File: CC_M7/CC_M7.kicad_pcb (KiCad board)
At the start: 4 copper layers, 40 x 65 mm, 118 parts, among them J1 Conn_01x04_Pin, J10 Conn_01x04_Pin, J11 USB_B_Micro, J12 Conn_01x04_Pin, J3 Conn_01x03_Pin, J4 Conn_01x03_Pin, J5 Conn_01x03_Pin, J6 Conn_01x03_Pin, J7 Conn_01x03_Pin, J8 Conn_01x03_Pin, U1 STM32H743VITx, U10 ME6211C33M5, U11 BMP581, U12 IIM-42652, U2 24AA64T-I/OT, U3 BMI088, U4 ICP-20100, U5 BMM150, U6 nRF52820-QDxx, U7 NRF21540-QDAA-R7, U8 TPS562246DRLR, U9 ME6211C33M5, Y1 32MHz, Y2 32MHz

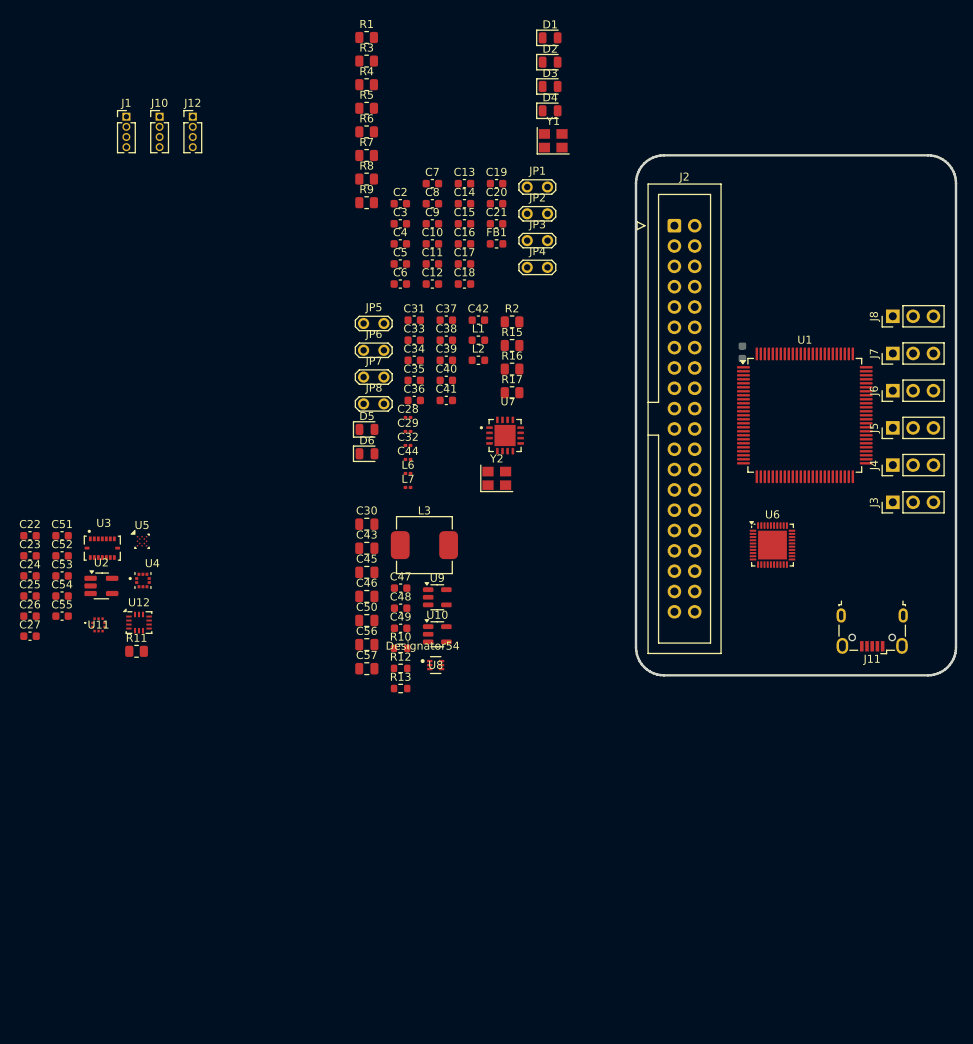
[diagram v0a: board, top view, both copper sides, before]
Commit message: nRF PCB placement completed
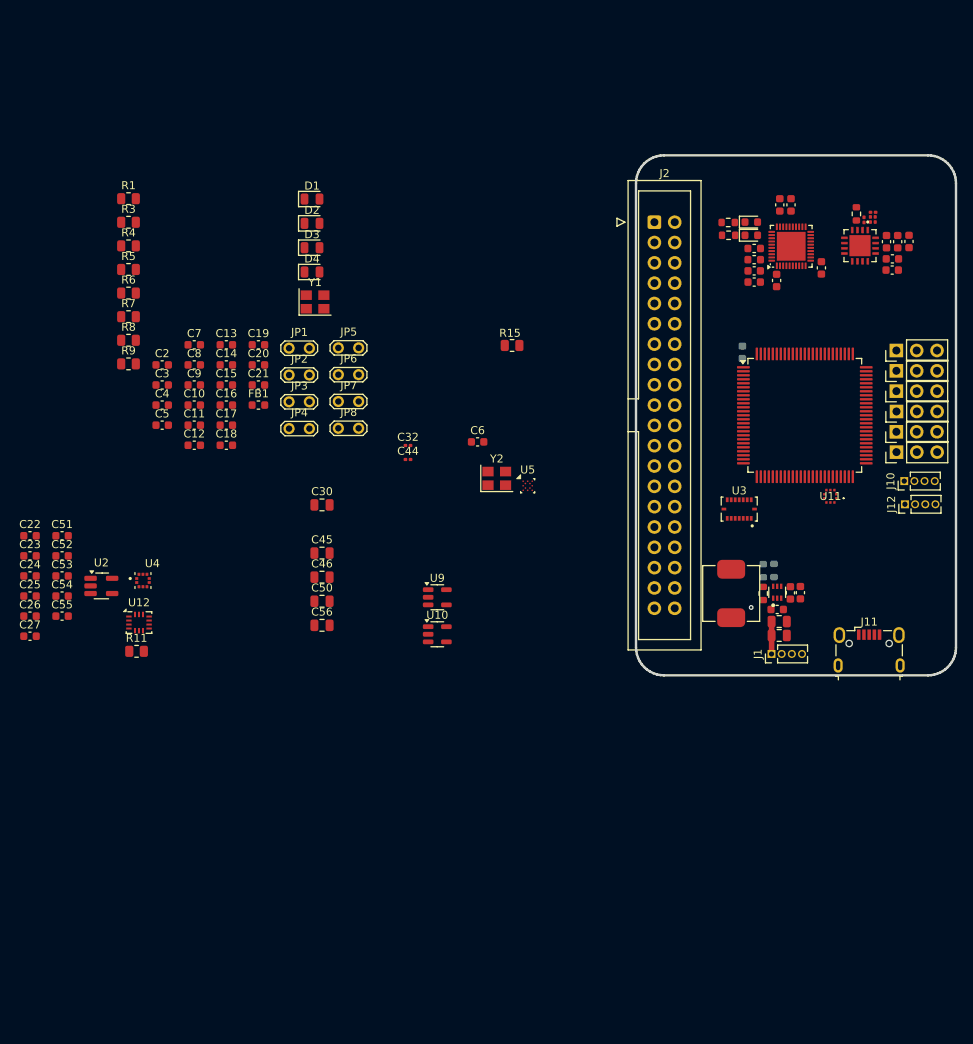
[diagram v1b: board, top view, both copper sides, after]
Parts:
- D5, D6: footprint LED_SMD:LED_0805_2012Metric -> LED_SMD:LED_0603_1608Metric
- R12, R13: moved to B.Cu
- R16, R17, R2: footprint Resistor_SMD:R_0805_2012Metric -> Resistor_SMD:R_0603_1608Metric
- moved J1 104.9 mm to (129.5, 130.8), turned to 90 degrees
- moved J10 103.6 mm to (146.1, 109.2), turned to 90 degrees
- moved J12 101.4 mm to (146.2, 112.1), turned to 90 degrees
- moved U11 92.9 mm to (136.9, 111.1), turned to 180 degrees
- moved U3 79.8 mm to (125.5, 112.7), turned to 180 degrees
- moved L7 66.8 mm to (141.9, 76.5), turned to 90 degrees
- moved L6 65.2 mm to (141.1, 76.5), turned to 90 degrees
- moved C29 64.3 mm to (142.2, 75.6)
- moved C28 63.4 mm to (142.5, 76.5), turned to 90 degrees
- moved C38 59.1 mm to (146.7, 79.2), turned to 90 degrees
- moved C40 59.0 mm to (145.3, 79.3), turned to -90 degrees
- moved C41 58.1 mm to (144.6, 82.8)
- moved C39 57.0 mm to (143.9, 79.3), turned to -90 degrees
- moved D6 56.1 mm to (127.0, 76.8)
- moved D5 53.8 mm to (127.0, 78.5)
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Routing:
- net +BATT: track 0.00 -> 4.16 mm
- net (no net): vias 0 -> 1

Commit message: Component placement completed
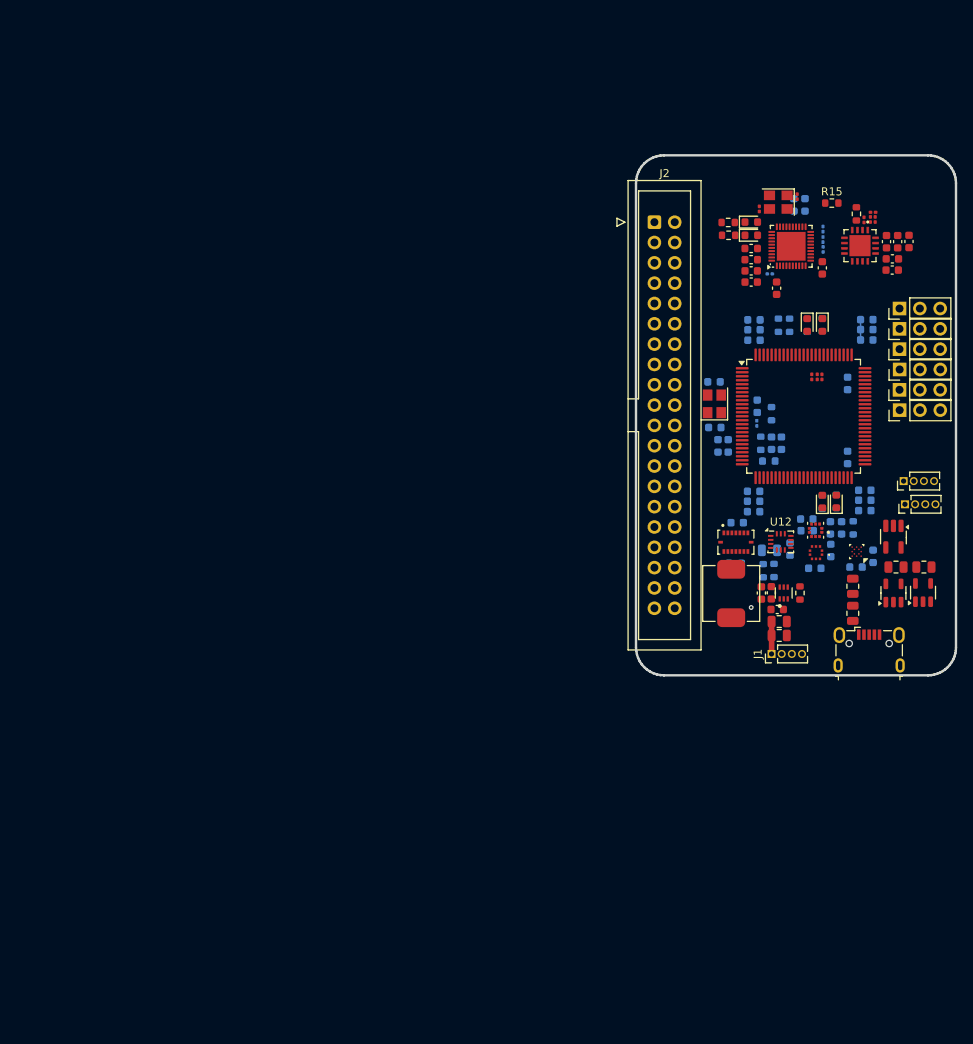
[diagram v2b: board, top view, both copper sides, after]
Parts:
- C10, C11, C12, C13, C14, C15, C16, C17, C18, C19, C2, C20, C21, C22, C23, C24, C25, C26, C27, C3, C31, C37, C4, C5, C51, C52, C53, C54, C55, C56, C6, C7, C8, C9, FB1: moved to B.Cu
- D1, D2, D3, D4: footprint LED_SMD:LED_0805_2012Metric -> LED_SMD:LED_0603_1608Metric
- JP1, JP2, JP3: footprint TestPoint:TestPoint_2Pads_Pitch2.54mm_Drill0.8mm -> Capacitor_SMD:C_0201_0603Metric
- JP4, JP5, JP6, JP7, JP8: footprint TestPoint:TestPoint_2Pads_Pitch2.54mm_Drill0.8mm -> Capacitor_SMD:C_0201_0603Metric; moved to B.Cu
- R1, R11, R3, R4, R5, R6, R7, R8, R9: footprint Resistor_SMD:R_0805_2012Metric -> Resistor_SMD:R_0603_1608Metric; moved to B.Cu
- R15: footprint Resistor_SMD:R_0805_2012Metric -> Resistor_SMD:R_0603_1608Metric
- moved C27 105.9 mm to (142.2, 118.6), turned to -90 degrees
- moved C26 103.4 mm to (140.1, 120.0)
- moved C23 101.5 mm to (138.3, 115.0), turned to -90 degrees
- moved C25 100.4 mm to (136.9, 115.0), turned to 90 degrees
- moved U2 99.2 mm to (144.8, 116.2), turned to -90 degrees
- moved C54 96.3 mm to (136.9, 117.9), turned to 90 degrees
- moved C55 94.3 mm to (134.9, 120.1), turned to 180 degrees
- moved C52 93.2 mm to (133.9, 114.0)
- moved C51 93.1 mm to (134.0, 115.4)
- moved C53 91.1 mm to (131.8, 117.7), turned to -90 degrees
- moved R11 90.9 mm to (139.8, 115.0), turned to 90 degrees
- moved R9 90.1 mm to (137.6, 111.7), turned to -90 degrees
- moved R8 89.1 mm to (135.9, 111.8), turned to -90 degrees
- moved C22 88.4 mm to (125.2, 114.4)
- moved C24 88.2 mm to (125.0, 119.5), turned to 180 degrees
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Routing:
- net +3.3V: track 0.00 -> 2.54 mm

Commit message: Mounting Hole added.
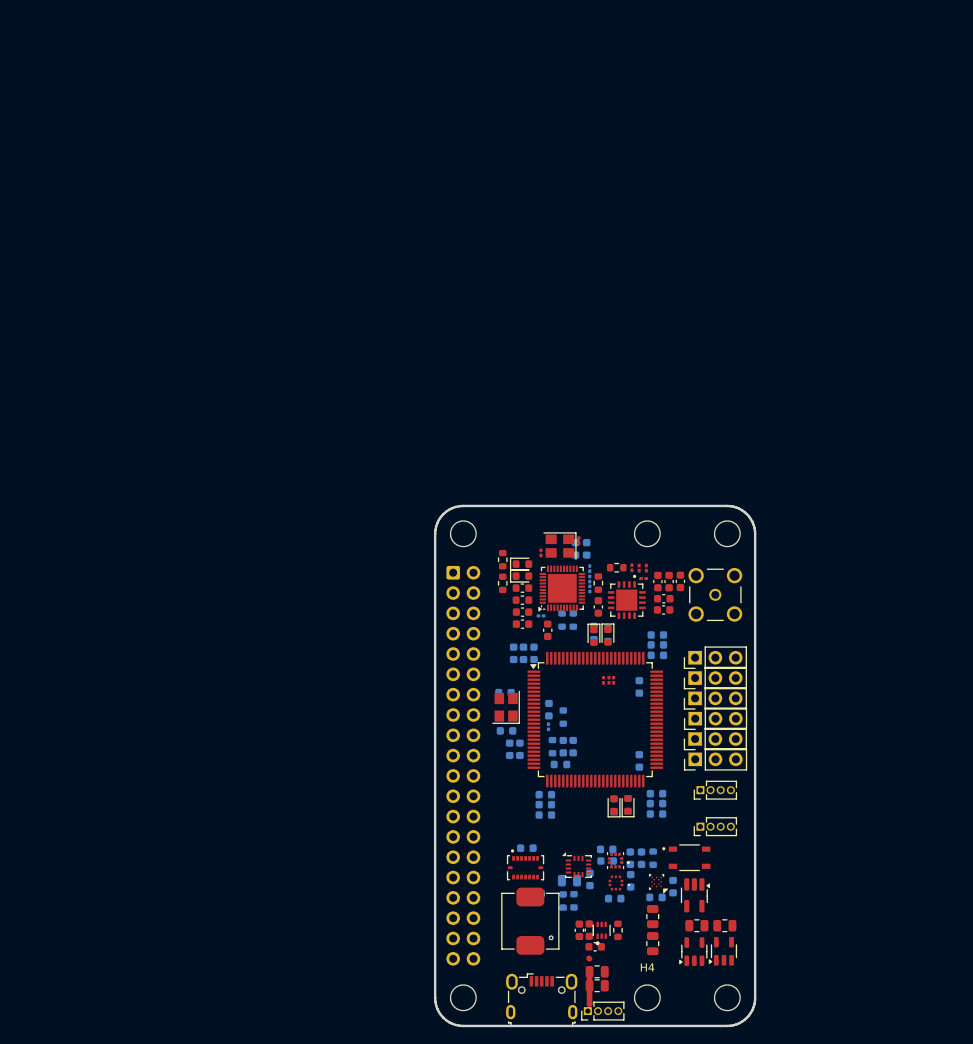
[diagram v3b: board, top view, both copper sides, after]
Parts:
- added H1: MountingHole, MountingHole:MountingHole_3.2mm_M3_ISO14580_Pad, F.Cu at (124.0, 173.8)
- added H2: MountingHole, MountingHole:MountingHole_3.2mm_M3_ISO14580_Pad, F.Cu at (91.0, 173.8)
- added H3: MountingHole, MountingHole:MountingHole_3.2mm_M3_ISO14580_Pad, F.Cu at (91.0, 115.8)
- added H4: MountingHole, MountingHole:MountingHole_3.2mm_M3_ISO14580_Pad, F.Cu at (114.0, 173.8)
- added H5: MountingHole, MountingHole:MountingHole_3.2mm_M3_ISO14580_Pad, F.Cu at (124.0, 115.8)
- added H6: MountingHole, MountingHole:MountingHole_3.2mm_M3_ISO14580_Pad, F.Cu at (114.0, 115.8)
- added J9: SMA_CONNECTOR, LPRS_SMA_CONNECTOR:LPRS_SMA_CONNECTOR, F.Cu at (122.5, 123.4)
- added S1: SKRPABE010, SW_SKRPABE010:SW_SKRPABE010, F.Cu at (119.3, 156.3)
- moved J11 59.6 mm to (100.8, 173.6)
- moved R15 55.8 mm to (107.9, 122.0), turned to -90 degrees
- moved C29 54.0 mm to (113.5, 121.4)
- moved R16 53.4 mm to (110.2, 120.0), turned to 180 degrees
- moved U7 53.0 mm to (111.4, 124.1)
- moved L7 52.3 mm to (113.0, 120.1), turned to -90 degrees
- moved L6 52.3 mm to (112.1, 120.0)
- moved C28 52.1 mm to (113.9, 120.1), turned to -90 degrees
- moved R2 51.9 mm to (95.9, 122.0), turned to 90 degrees
- moved JP8 51.5 mm to (106.8, 122.7)
- moved JP6 51.5 mm to (106.8, 120.1)
- moved JP7 51.5 mm to (106.8, 121.5)
- moved JP5 51.4 mm to (100.7, 126.1)
- moved C35 51.4 mm to (101.6, 127.8)
- moved U6 51.4 mm to (103.4, 122.6)
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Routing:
- net +3.3V: track 2.54 -> 0.00 mm

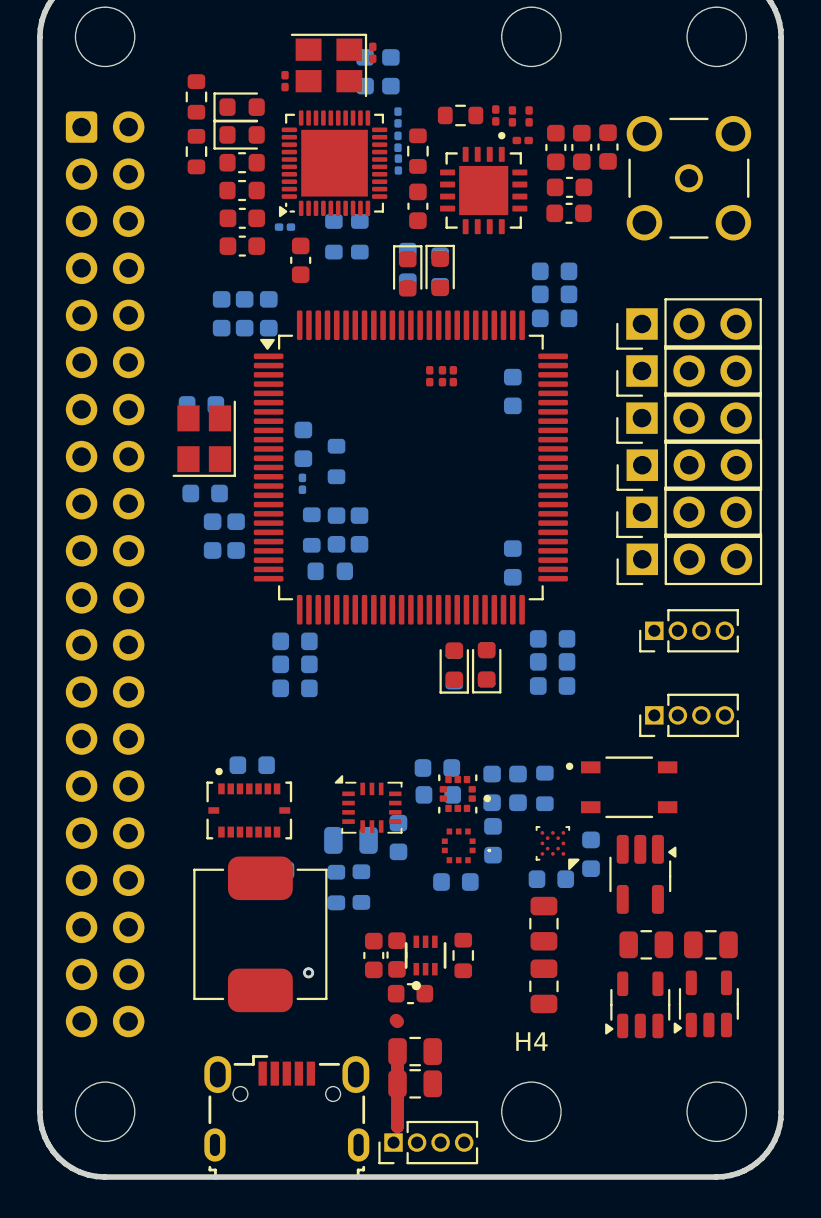
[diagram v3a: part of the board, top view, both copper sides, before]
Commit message: 1x04 connectors chosen and added
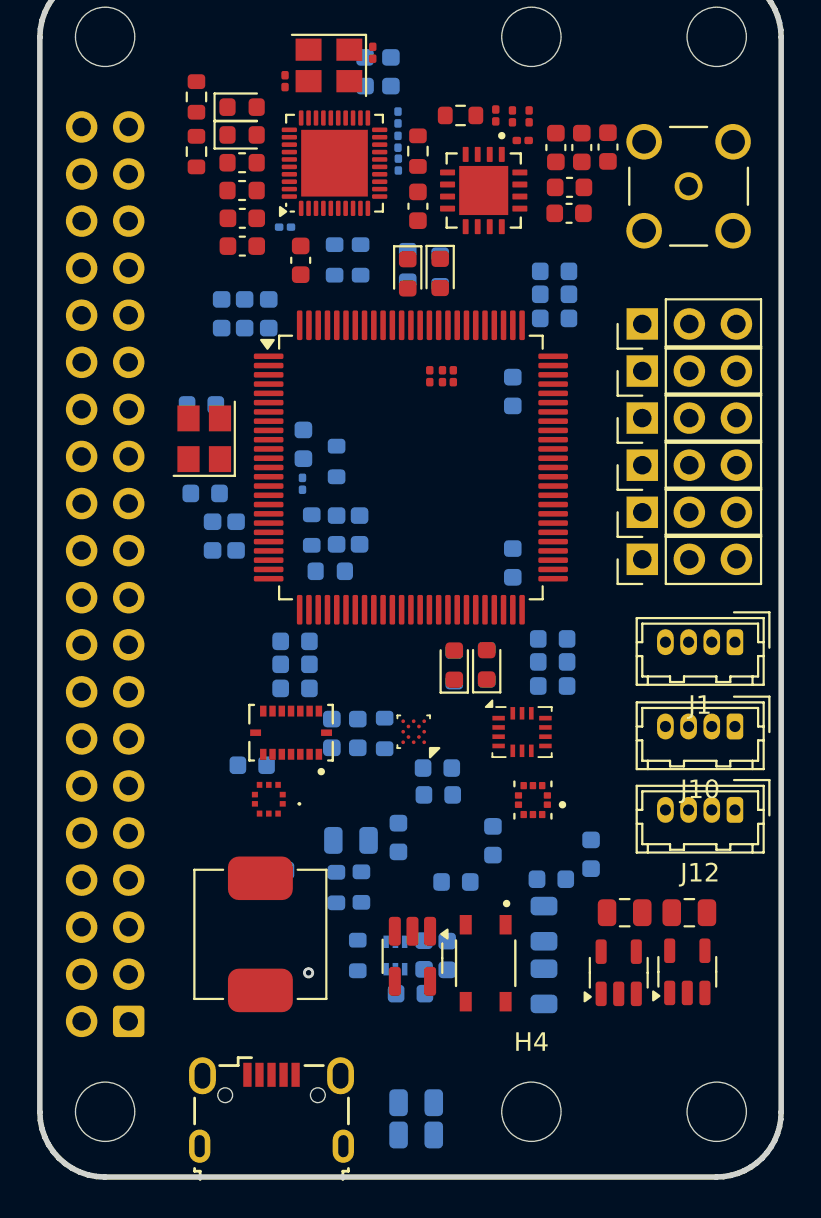
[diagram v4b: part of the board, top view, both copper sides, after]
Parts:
- C30, C43, C46, C47, C48, C49, C57, R10, U8: moved to B.Cu
- J1, J10, J12: footprint Connector_PinHeader_1.27mm:PinHeader_1x04_P1.27mm_Vertical -> Connector_Hirose:Hirose_DF13-04P-1.25DSA_1x04_P1.25mm_Vertical
- moved J2 48.3 mm to (92.3, 168.9), turned to 180 degrees
- moved J1 32.7 mm to (125.0, 148.4), turned to 180 degrees
- moved U2 13.1 mm to (107.6, 165.4)
- moved S1 12.3 mm to (111.5, 165.8), turned to -90 degrees
- moved U11 10.5 mm to (99.8, 156.9)
- moved U5 9.63 mm to (107.7, 153.3)
- moved R11 9.14 mm to (106.1, 153.4)
- moved C23 9.14 mm to (104.7, 153.4)
- moved C25 9.14 mm to (103.2, 153.4)
- moved U12 9.07 mm to (113.5, 153.3)
- moved J10 6.75 mm to (125.0, 153.0), turned to 180 degrees
- moved J12 6.70 mm to (125.0, 157.5), turned to 180 degrees
- moved R10 5.69 mm to (104.6, 165.4)
- moved U3 4.76 mm to (101.0, 153.3), turned to 180 degrees
- moved U4 4.07 mm to (114.1, 157.0)
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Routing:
- net +BATT: track 4.16 -> 0.00 mm

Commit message: constraints set
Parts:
- JP1, JP2, JP3: moved to B.Cu
- moved JP3 1.47 mm to (110.0, 134.1)
- moved JP1 1.35 mm to (108.5, 134.1)
- moved C29 0.40 mm to (113.4, 121.0)
- moved C39 0.27 mm to (115.2, 121.5)
- moved C40 0.27 mm to (116.6, 121.5)
- moved C38 0.25 mm to (118.0, 121.5)
- moved C28 0.25 mm to (113.9, 119.8)
- moved L7 0.25 mm to (113.0, 119.8)
- moved C32 0.24 mm to (105.7, 116.6)
- moved C44 0.23 mm to (100.5, 118.2)
- moved R17 0.08 mm to (95.9, 119.0)

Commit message: impadance control check and track thickness added
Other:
- board text added: "(usb trace spacing = 0.2032)"

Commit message: Schematic pdf added.
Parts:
- added J13: Batt_Pins, Connector_Molex:Molex_KK-254_AE-6410-02A_1x02_P2.54mm_Vertical, F.Cu at (106.8, 173.7)
- moved C43 4.00 mm to (107.7, 171.0)
- moved C57 4.00 mm to (107.7, 169.3)

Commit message: [200~
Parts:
- C32, C44: footprint Capacitor_SMD:C_0201_0603Metric -> Capacitor_SMD:C_0603_1608Metric; moved to B.Cu
- C35, C38, C39, C40, R17, R2: moved to B.Cu
- U8: moved to F.Cu
- moved C19 44.3 mm to (145.4, 145.2), turned to 180 degrees
- moved J13 42.0 mm to (148.8, 173.9), turned to 90 degrees
- moved S1 38.7 mm to (145.5, 147.3)
- moved C43 36.9 mm to (144.5, 172.7), turned to -90 degrees
- moved R10 36.3 mm to (140.8, 162.8)
- moved C57 35.3 mm to (142.7, 172.7), turned to -90 degrees
- moved R13 33.0 mm to (135.9, 172.8)
- moved U8 32.8 mm to (138.7, 172.8), turned to 180 degrees
- moved R12 30.4 mm to (133.8, 163.0), turned to 0 degrees
- moved C49 25.9 mm to (133.9, 161.5), turned to 180 degrees
- moved C48 25.9 mm to (134.2, 172.8)
- moved C47 24.4 mm to (130.4, 176.0)
- moved D4 24.2 mm to (108.8, 173.7)
- moved D3 24.2 mm to (107.2, 173.7)
- moved R9 24.1 mm to (108.8, 173.6)
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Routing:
- net (no net): vias 1 -> 0
- added copper zone on In2.Cu, net +3.3V
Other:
- outline, holes or cut-outs redrawn
- board text removed: "(usb trace spacing = 0.2032)"
